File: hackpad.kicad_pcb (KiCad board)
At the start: 2 copper layers, 60 x 65 mm, 9 parts, among them J1 Conn_01x04, SW1 SW_Push, SW2 SW_Push, SW3 SW_Push, SW4 SW_Push, SW5 SW_Push, SW6 SW_Push, SW7 SW_Push, U1 MOUDLE-SEEEDUINO-XIAO

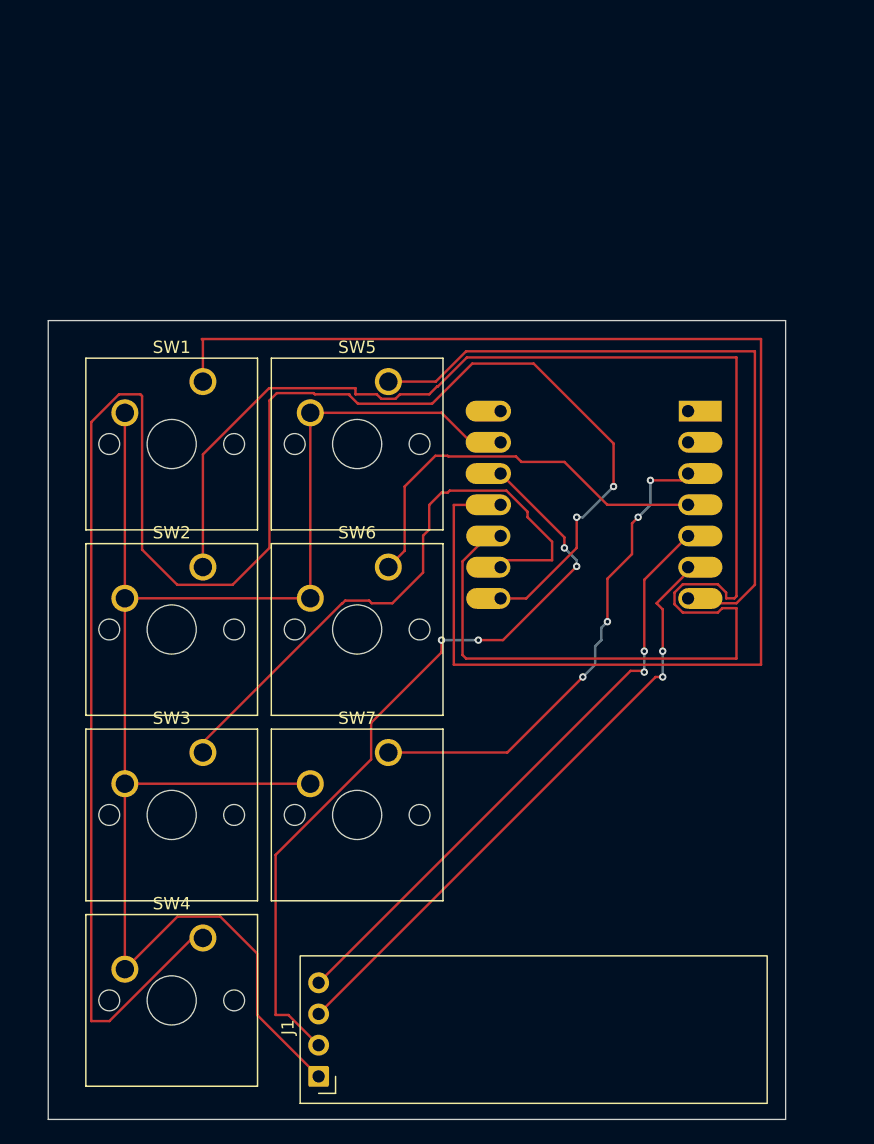
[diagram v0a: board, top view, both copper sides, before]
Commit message: update pcb, add case files
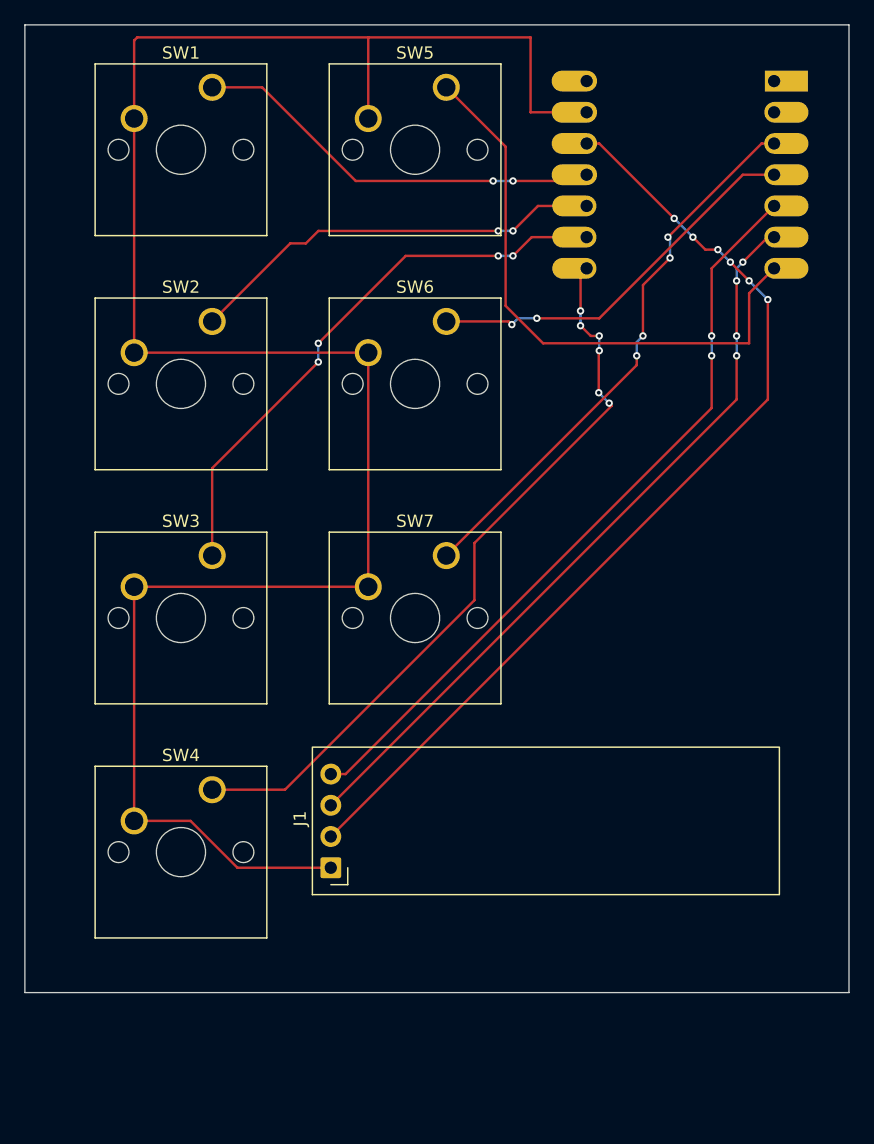
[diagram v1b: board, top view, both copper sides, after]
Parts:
- moved U1 27.8 mm to (154.9, 40.1)
- moved SW5 24.4 mm to (135.9, 33.0)
- moved SW1 24.0 mm to (116.8, 33.0)
- moved SW6 20.5 mm to (135.9, 52.1)
- moved SW2 20.0 mm to (116.8, 52.1)
- moved J1 17.0 mm to (126.5, 96.5)
- moved SW7 16.7 mm to (135.9, 71.1)
- moved SW3 16.0 mm to (116.8, 71.1)
- moved SW4 12.1 mm to (116.8, 90.2)
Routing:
- net Net-(U1-PB09_A7_D7_RX): track 153.7 -> 61.1 mm, vias 2 -> 6
- net Net-(U1-PA5_A9_D9_MISO): track 126.9 -> 34.4 mm, vias 0 -> 2
- net Net-(U1-PA6_A10_D10_MOSI): track 117.3 -> 33.8 mm, vias 0 -> 2
- net GND: track 132.9 -> 168.8 mm
- net Net-(J1-Pin_2): track 64.2 -> 78.4 mm, vias 4 -> 6
- net Net-(J1-Pin_4): track 49.6 -> 61.9 mm
- net Net-(J1-Pin_3): track 49.6 -> 61.5 mm, vias 2 -> 4
- net Net-(U1-PB08_A6_D6_TX): track 56.1 -> 47.8 mm
- net Net-(U1-PA10_A2_D2): track 39.9 -> 45.3 mm
- net Net-(U1-PA7_A8_D8_SCK): track 48.7 -> 46.3 mm, vias 0 -> 4
- net Net-(U1-PA11_A3_D3): track 32.9 -> 31.8 mm, vias 0 -> 2
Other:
- board size 60 x 65 mm -> 67.1 x 78.7 mm
